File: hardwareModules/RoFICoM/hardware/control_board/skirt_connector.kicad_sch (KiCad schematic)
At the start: 22 parts, among them J10 SENSE_A, J11 SENSE_B, J12 SENSE_1, J13 SENSE_2, J14 48V_A, J15 48V_1, J16 48V_B, J17 48V_2, J18 GND_A, J19 GND_1, J20 GND_B, J21 GND_2, J22 RX_A, J23 RX_B, J24 TX_1, J25 TX_2, U8 VL53L1X

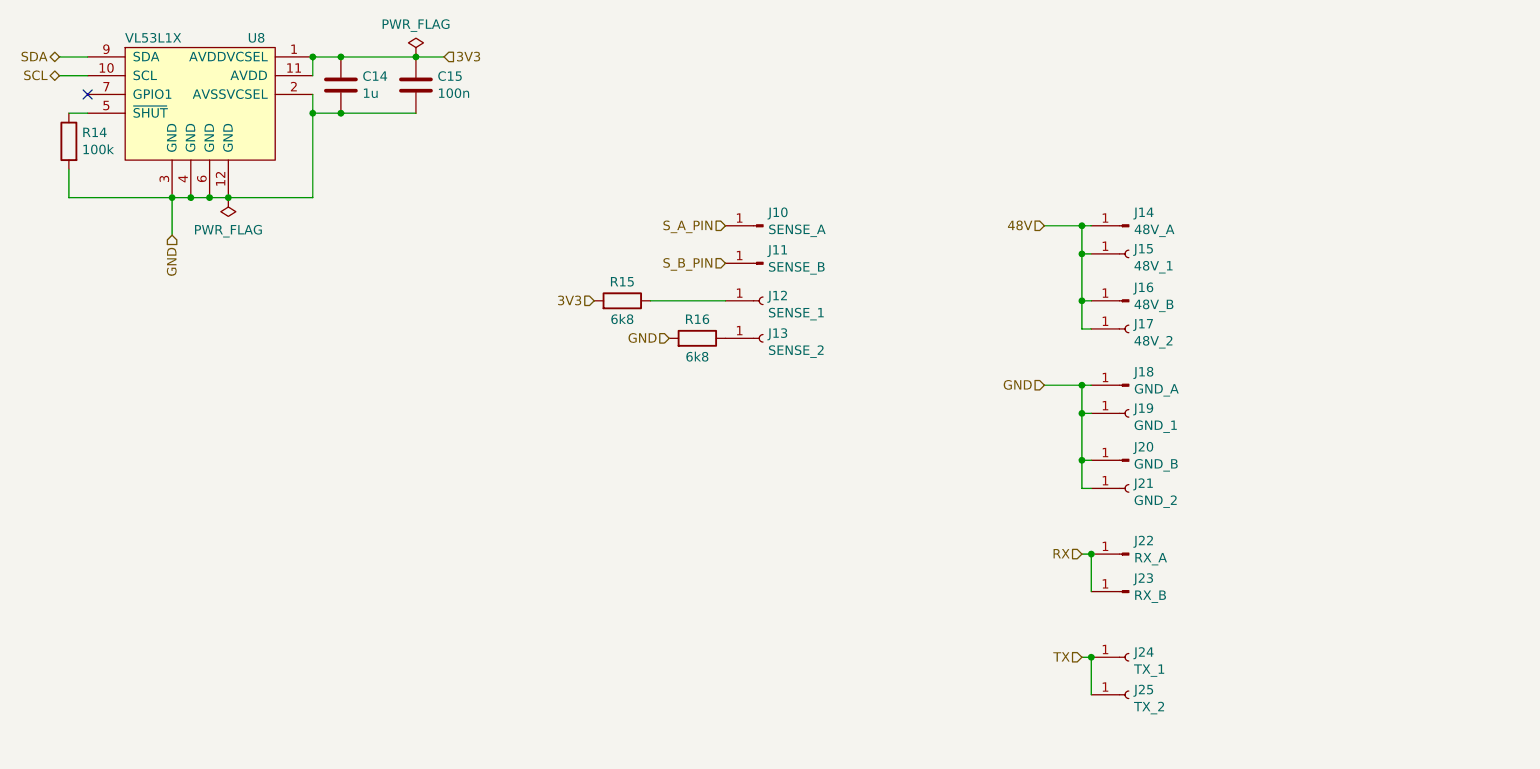
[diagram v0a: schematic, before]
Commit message: roficom: Implement v1 hardware
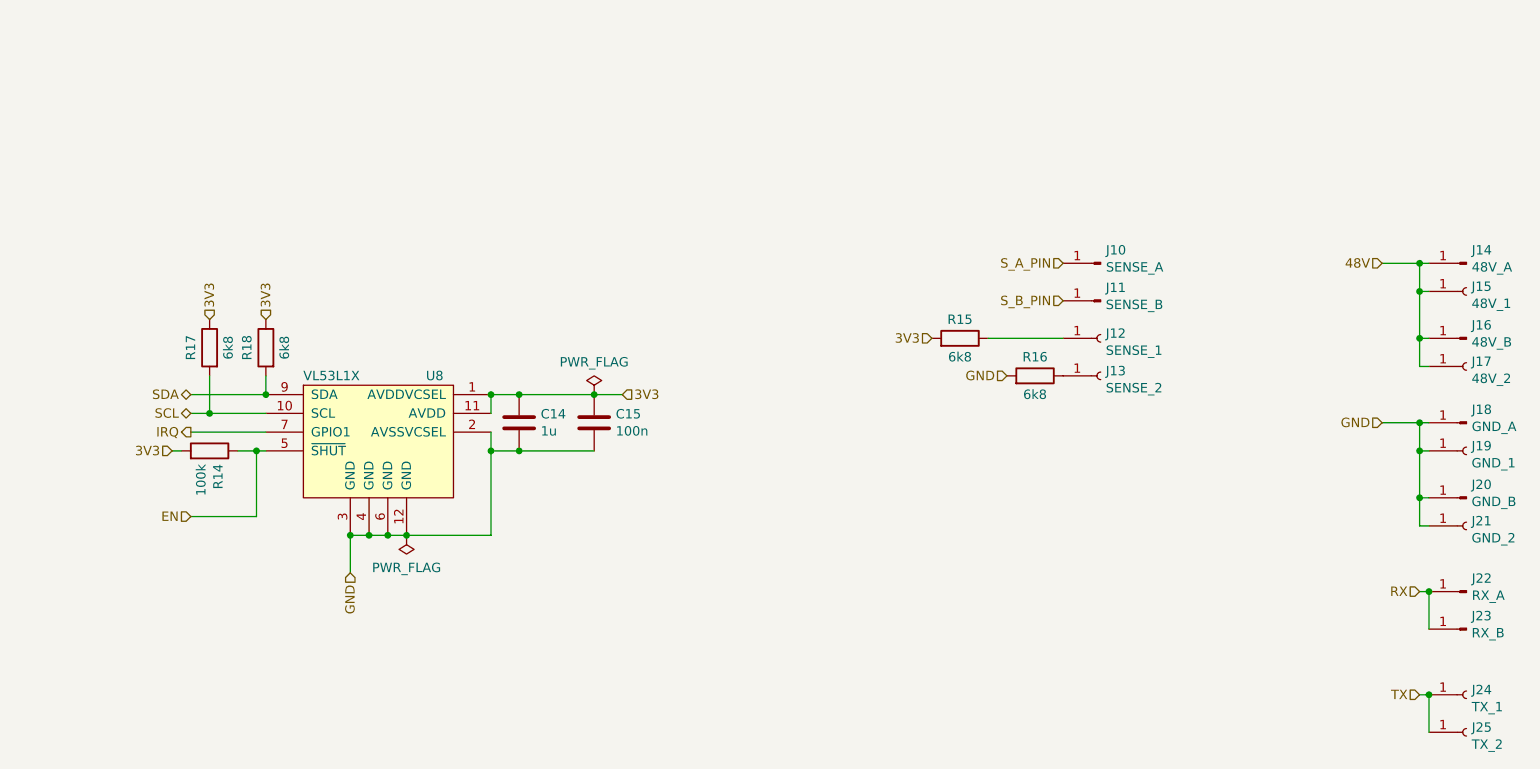
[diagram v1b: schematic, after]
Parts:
- added R17, R18: 6k8, Resistor_SMD:R_0402_1005Metric, symbol Device:R
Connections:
- net 3V3: now also R14.2, R17.1, R18.1
- net GND: no longer R14.2
- net SCL: now also R17.2
- net SDA: now also R18.2
- net EN: now reaches R14.1, U8.5 (~{SHUT})
- net IRQ: now reaches U8.7 (GPIO1)
- no-connect marks 1 -> 0
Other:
- moved on the sheet: C14, C15, J10, J11, J12, J13, J14, J15, J16, J17, J18, J19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

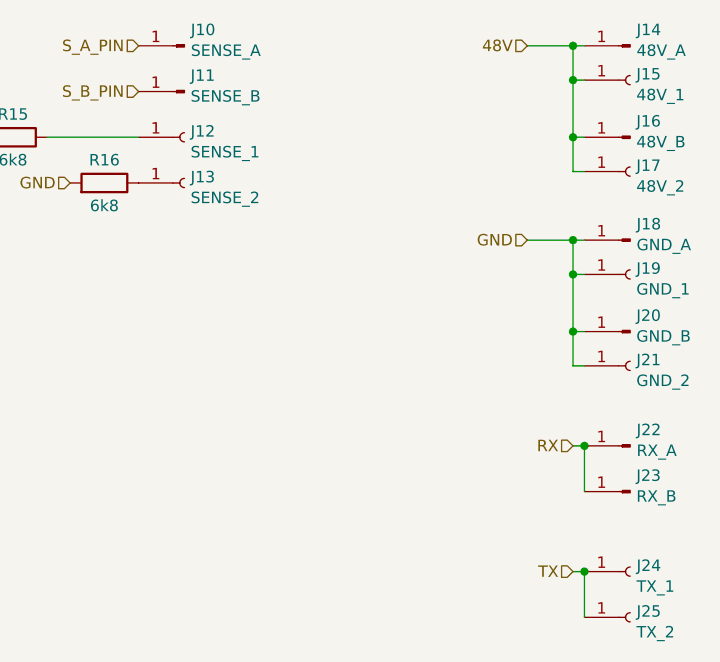
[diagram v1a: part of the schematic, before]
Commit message: hardware: Add custom FPC cables
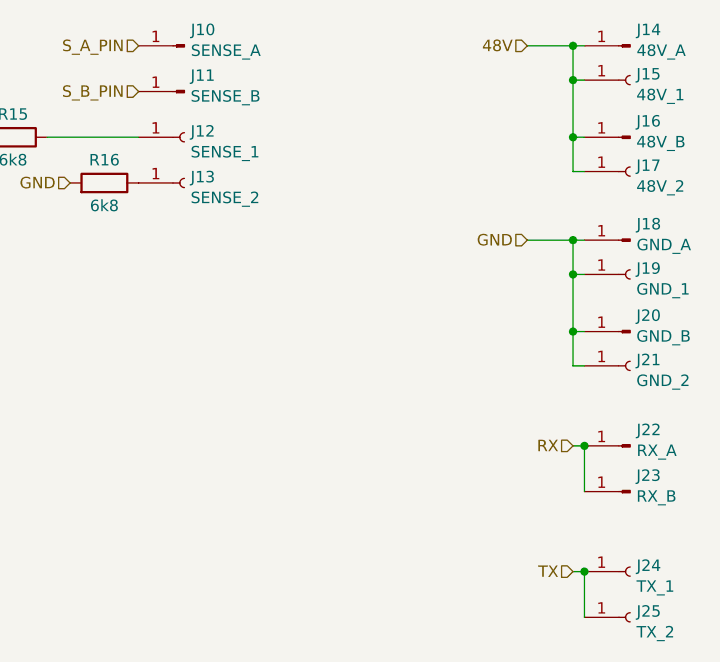
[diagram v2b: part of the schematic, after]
